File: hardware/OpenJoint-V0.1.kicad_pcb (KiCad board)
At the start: 2 copper layers, 42 x 42 mm, 14 parts, among them J1 TYPE-C-31-M-12, J2 Screw_Terminal_01x08, J4 Screw_Terminal_01x04, J6 Screw_Terminal_01x06, U1 ESP32-C3-MINI-1-H4, U2 AS5600, U3 SN65HVD230, U4 AMS1117-3.3

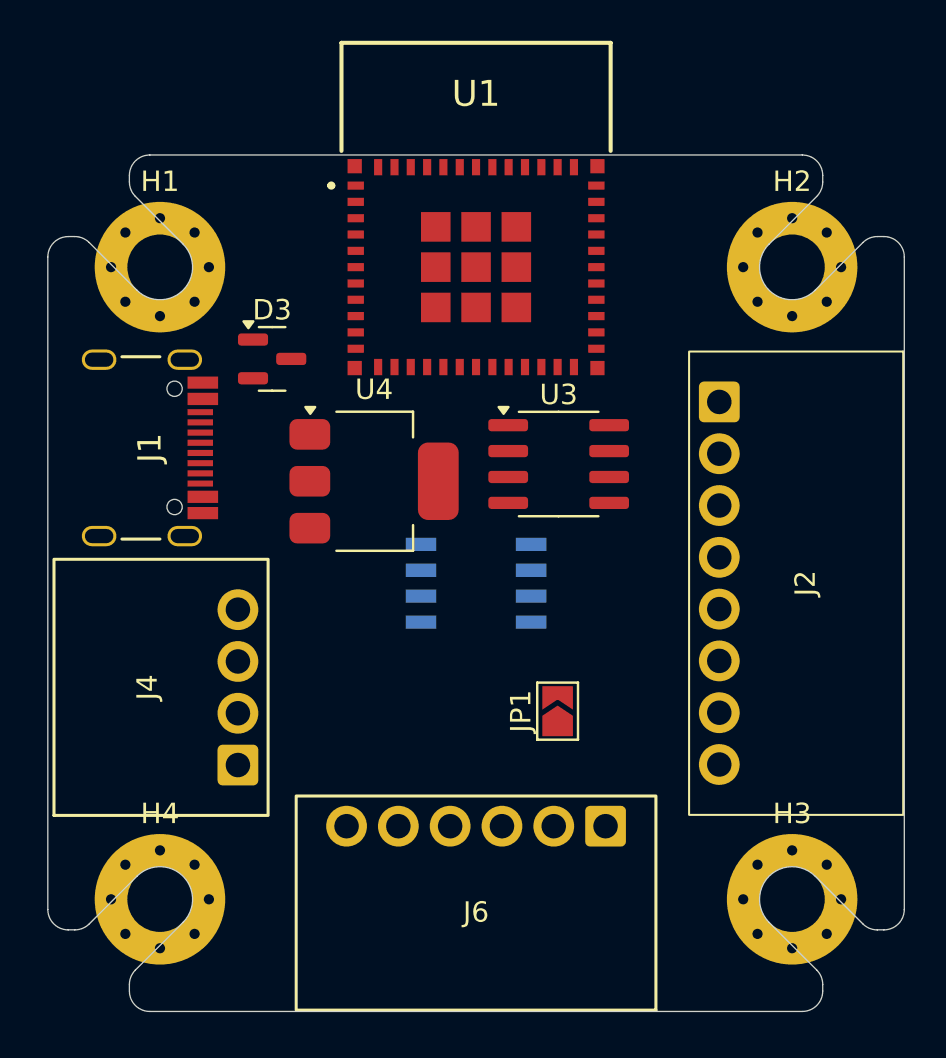
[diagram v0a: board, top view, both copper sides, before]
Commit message: feat: Complete footprint assignment and component placement
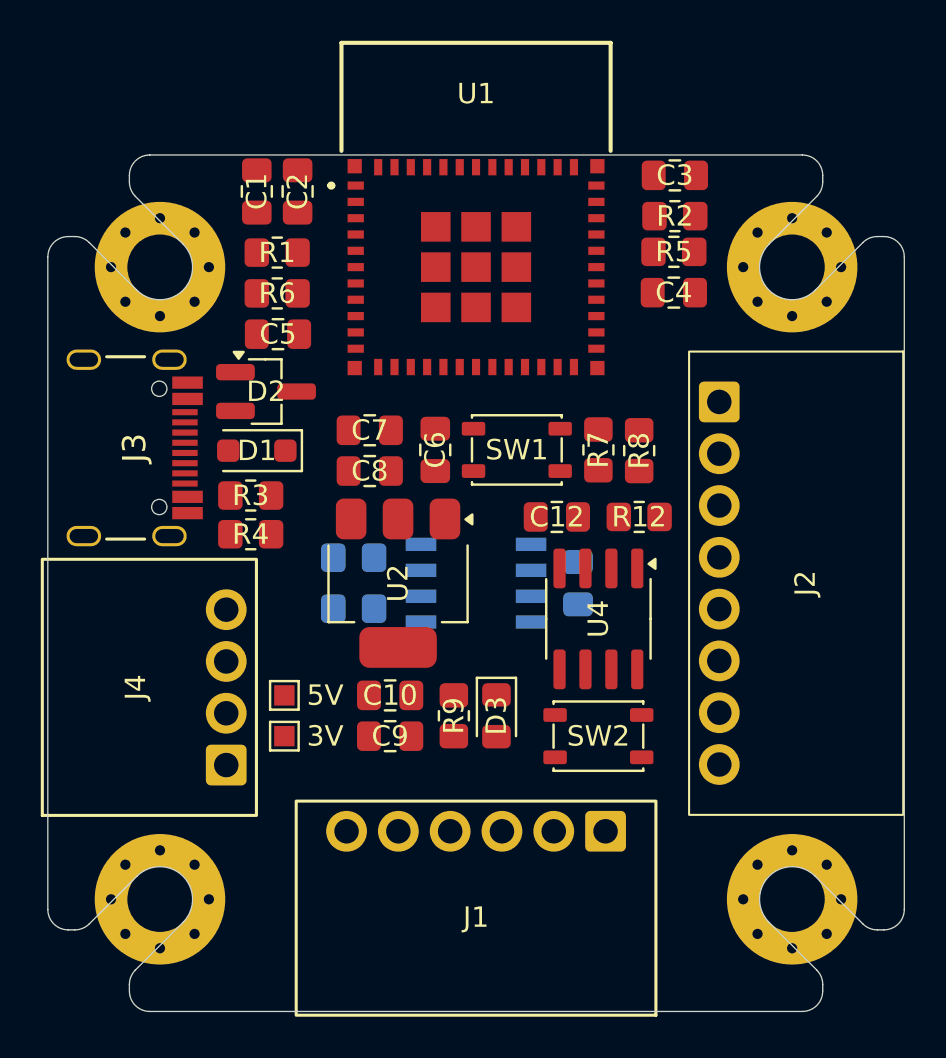
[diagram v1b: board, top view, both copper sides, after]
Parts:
- removed J6: Screw_Terminal_01x06, footprint:TerminalBlock_Xinya_2.54-6P_1x06_P2.54mm_Horizontal
- removed JP1: SolderJumper_2_Open, Jumper:SolderJumper-2_P1.3mm_Open_TrianglePad1.0x1.5mm
- added 3V: TestPoint, TestPoint:TestPoint_Pad_1.0x1.0mm, F.Cu at (90.6, 107.5)
- added 5V: TestPoint, TestPoint:TestPoint_Pad_1.0x1.0mm, F.Cu at (90.6, 105.5)
- added C1: 10u, Capacitor_SMD:C_0805_2012Metric_Pad1.18x1.45mm_HandSolder, F.Cu at (89.2, 80.8)
- added C10: 10u, Capacitor_SMD:C_0805_2012Metric_Pad1.18x1.45mm_HandSolder, F.Cu at (95.8, 105.5)
- added C11: 1u, Capacitor_SMD:C_0805_2012Metric_Pad1.18x1.45mm_HandSolder, B.Cu at (105.0, 100.0)
- added C12: 0.1u, Capacitor_SMD:C_0805_2012Metric_Pad1.18x1.45mm_HandSolder, F.Cu at (104.0, 96.8)
- added C2: 0.1u, Capacitor_SMD:C_0805_2012Metric_Pad1.18x1.45mm_HandSolder, F.Cu at (91.2, 80.8)
- added C3: 1u, Capacitor_SMD:C_0805_2012Metric_Pad1.18x1.45mm_HandSolder, F.Cu at (109.8, 80.0)
- added C4: 1u, Capacitor_SMD:C_0805_2012Metric_Pad1.18x1.45mm_HandSolder, F.Cu at (109.7, 85.8)
- added C5: 1u, Capacitor_SMD:C_0805_2012Metric_Pad1.18x1.45mm_HandSolder, F.Cu at (90.3, 87.8)
- added C6: 0.1u, Capacitor_SMD:C_0805_2012Metric_Pad1.18x1.45mm_HandSolder, F.Cu at (98.0, 93.5)
- added C7: 10u, Capacitor_SMD:C_0805_2012Metric_Pad1.18x1.45mm_HandSolder, F.Cu at (94.8, 92.5)
- added C8: 1u, Capacitor_SMD:C_0805_2012Metric_Pad1.18x1.45mm_HandSolder, F.Cu at (94.8, 94.5)
- added C9: 1u, Capacitor_SMD:C_0805_2012Metric_Pad1.18x1.45mm_HandSolder, F.Cu at (95.8, 107.5)
- added D1: SS210, Diode_SMD:D_SOD-123F, F.Cu at (89.2, 93.5)
- added D2: NUP2105L, Package_TO_SOT_SMD:SOT-23_Handsoldering, F.Cu at (89.7, 90.6)
- added J3: TYPE-C-31-M-12, footprint:USB-TYPE-C-31-M-12, F.Cu at (83.2, 93.4)
- added R1: 10k, Resistor_SMD:R_0805_2012Metric_Pad1.20x1.40mm_HandSolder, F.Cu at (90.2, 83.8)
- added R10: 4.7k, Resistor_SMD:R_0805_2012Metric_Pad1.20x1.40mm_HandSolder, B.Cu at (94.0, 98.8)
- added R11: 4.7k, Resistor_SMD:R_0805_2012Metric_Pad1.20x1.40mm_HandSolder, B.Cu at (94.0, 101.2)
- added R12: 4.7k, Resistor_SMD:R_0805_2012Metric_Pad1.20x1.40mm_HandSolder, F.Cu at (108.0, 96.8)
- added R2: 0, Resistor_SMD:R_0805_2012Metric_Pad1.20x1.40mm_HandSolder, F.Cu at (109.8, 82.0)
- added R3: 5.1k, Resistor_SMD:R_0805_2012Metric_Pad1.20x1.40mm_HandSolder, F.Cu at (89.0, 95.7)
- added R4: 5.1k, Resistor_SMD:R_0805_2012Metric_Pad1.20x1.40mm_HandSolder, F.Cu at (89.0, 97.6)
- added R5: 0, Resistor_SMD:R_0805_2012Metric_Pad1.20x1.40mm_HandSolder, F.Cu at (109.7, 83.8)
- added R6: 10k, Resistor_SMD:R_0805_2012Metric_Pad1.20x1.40mm_HandSolder, F.Cu at (90.2, 85.8)
- added R7: 0, Resistor_SMD:R_0805_2012Metric_Pad1.20x1.40mm_HandSolder, F.Cu at (106.0, 93.5)
- added R8: 10k, Resistor_SMD:R_0805_2012Metric_Pad1.20x1.40mm_HandSolder, F.Cu at (108.0, 93.5)
- added R9: 1k, Resistor_SMD:R_0805_2012Metric_Pad1.20x1.40mm_HandSolder, F.Cu at (98.9, 106.5)
- added SW1: SW_Push, SamacSys_Parts:SW_SPST_PTS810, F.Cu at (102.0, 93.5)
- added SW2: SW_Push, SamacSys_Parts:SW_SPST_PTS810, F.Cu at (106.0, 107.5)
- D3: value NUP2105L -> LED_Small; footprint Package_TO_SOT_SMD:SOT-23 -> LED_SMD:LED_0805_2012Metric_Pad1.15x1.40mm_HandSolder
- J1: value TYPE-C-31-M-12 -> Screw_Terminal_01x06; footprint footprint:USB-TYPE-C-31-M-12 -> footprint:TerminalBlock_Xinya_2.54-6P_1x06_P2.54mm_Horizontal
- U2: value AS5600 -> AMS1117-3.3; footprint SamacSys_Parts:SOIC127P600X175-8N -> Package_TO_SOT_SMD:SOT-223-3_TabPin2; moved to F.Cu
- U3: value SN65HVD230 -> AS5600; footprint Package_SO:SOIC-8_3.9x4.9mm_P1.27mm -> SamacSys_Parts:SOIC127P600X175-8N; moved to B.Cu
- U4: value AMS1117-3.3 -> SN65HVD230; footprint Package_TO_SOT_SMD:SOT-223-3_TabPin2 -> Package_SO:SOIC-8_3.9x4.9mm_P1.27mm
- moved J1 29.2 mm to (106.3, 112.2), turned to 180 degrees
- moved D3 20.7 mm to (101.0, 106.5), turned to -90 degrees
- moved U4 12.9 mm to (106.0, 101.8), turned to -90 degrees
- moved U3 7.11 mm to (100.0, 100.0), turned to 180 degrees
- moved U2 3.83 mm to (96.2, 100.0), turned to -90 degrees
- moved J4 0.57 mm to (87.8, 108.9)
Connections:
- D3 pad 1: /USB_D- -> GND
- D3 pad 2: /USB_D+ -> Net-(D3-A)
- J2 pad 5: /SCK -> /GPIO0
- J2 pad 6: /MISO -> /GPIO1
- J2 pad 7: /MOSI -> /GPIO2
- J2 pad 8: /CS -> /GPIO3
- U1 pad 12: /IO0 -> /GPIO0
- U1 pad 13: /IO1 -> /GPIO1
- U1 pad 18: /IO4 -> /GPIO3
- U1 pad 6: /IO3 -> /GPIO2
- U2 pad 1: unconnected-(U2-5V-Pad1) -> GND
- U2 pad 3: unconnected-(U2-OUT-Pad3) -> +5V
- U3 pad 1: /CAN_TX -> unconnected-(U3-5V-Pad1)
- U3 pad 2: GND -> +3V3
- U3 pad 3: +3V3 -> unconnected-(U3-OUT-Pad3)
- U3 pad 4: /CAN_RX -> GND
- U3 pad 5: unconnected-(U3-Vref-Pad5) -> GND
- U3 pad 6: /CAN_N -> /EN_SDA
- U3 pad 7: /CAN_P -> /EN_SCL
- U3 pad 8: Net-(U3-Rs) -> GND
- U4 pad 1: GND -> /CAN_TX
- U4 pad 2: +3V3 -> GND
- U4 pad 3: +5V -> +3V3
